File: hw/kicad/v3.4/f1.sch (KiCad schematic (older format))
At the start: 15 parts

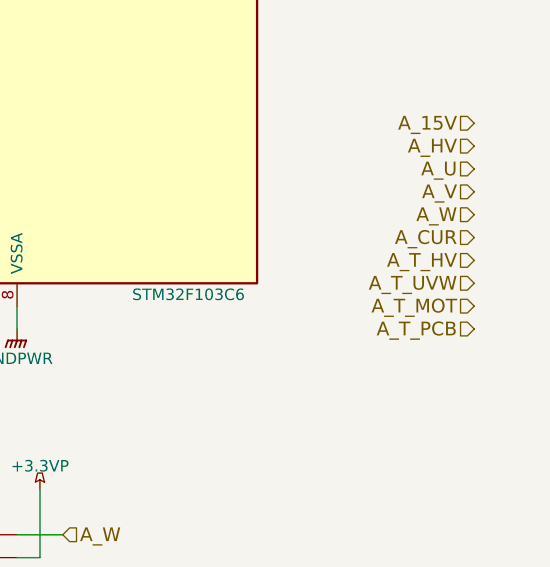
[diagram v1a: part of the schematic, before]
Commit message: +iram256
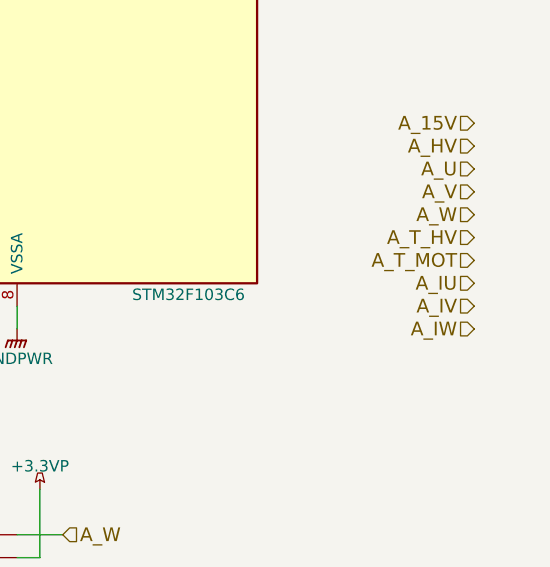
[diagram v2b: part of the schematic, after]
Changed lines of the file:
@@
 $Descr A4 11693 8268
 encoding utf-8
-Sheet 3 14
+Sheet 3 15
 Title ""
 Date ""
@@
 Text HLabel 8000 4900 0    60   Input ~ 0
 A_W
+Text HLabel 8000 5200 0    60   Input ~ 0
+A_IU
 Text HLabel 8000 5000 0    60   Input ~ 0
-A_CUR
+A_T_HV
 Text HLabel 8000 5100 0    60   Input ~ 0
-A_T_HV
-Text HLabel 8000 5200 0    60   Input ~ 0
-A_T_UVW
-Text HLabel 8000 5300 0    60   Input ~ 0
 A_T_MOT
-Text HLabel 8000 5400 0    60   Input ~ 0
-A_T_PCB
 Text HLabel 7400 3400 2    60   Input ~ 0
 HV_EN
@@
 	0    1    1    0
 $EndComp
+Text HLabel 8000 5300 0    60   Input ~ 0
+A_IV
+Text HLabel 8000 5400 0    60   Input ~ 0
+A_IW
 $EndSCHEMATC

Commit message: hw v3.4
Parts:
- added U?: USBLC6-4SC6, symbol USBLC6-4SC6
- R?: value 1k -> 10k
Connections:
- net +3.3VP: now also U?.5 (VBUS)
- net A_IU: now also U?.1 (I/O1)
- net A_IV: now also U?.3 (I/O2)
- net A_IW: now also U?.6 (I/O4)
- net A_T_MOT: now also U?.4 (I/O3)
- net GNDPWR: now also U?.2 (GND)
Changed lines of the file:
@@
 EESchema Schematic File Version 2
 LIBS:conn
+LIBS:power
 LIBS:stmbl_3.4-cache
 EELAYER 25 0
@@
 	1    0    0    -1
 $EndComp
-Wire Wire Line
-	5400 1700 5400 1900
-Wire Wire Line
-	5500 1700 5500 1900
-Wire Wire Line
-	5700 1700 5700 1900
-Wire Wire Line
-	6000 1700 6000 1900
-Wire Wire Line
-	5150 1400 6000 1400
-Connection ~ 5700 1400
-Connection ~ 5500 1400
 $Comp
 L GNDPWR #PWR?
@@
 	1    0    0    -1
 $EndComp
-Wire Wire Line
-	5150 1500 5150 1400
-Connection ~ 5400 1400
 $Comp
 L +3.3VP #PWR?
@@
 	1    0    0    -1
 $EndComp
-Wire Wire Line
-	6200 1700 6200 1800
-Wire Wire Line
-	6200 1800 6000 1800
-Connection ~ 6000 1800
 $Comp
 L C C?
@@
 	0    1    1    0
 $EndComp
-Wire Wire Line
-	3400 2800 3500 2800
-Wire Wire Line
-	3400 2500 3500 2500
-Wire Wire Line
-	3800 2500 4100 2500
-Wire Wire Line
-	3800 2800 4100 2800
-Wire Wire Line
-	4100 2800 4100 2700
-Wire Wire Line
-	4100 2700 4200 2700
-Connection ~ 3900 2800
-Wire Wire Line
-	4200 2600 4100 2600
-Wire Wire Line
-	4100 2600 4100 2500
-Connection ~ 3900 2500
 $Comp
 L C C?
@@
 	1    0    0    -1
 $EndComp
-Wire Wire Line
-	3500 2900 4200 2900
-Wire Wire Line
-	3500 2900 3500 3050
 $Comp
 L GNDPWR #PWR?
@@
 	1    0    0    -1
 $EndComp
-Wire Wire Line
-	3500 3450 3500 3350
 $Comp
 L +3.3VP #PWR?
@@
 	-1   0    0    1
 $EndComp
-Wire Wire Line
-	3800 3000 3800 2900
-Connection ~ 3800 2900
 $Comp
 L C C?
@@
 	0    1    1    0
 $EndComp
-Wire Wire Line
-	4000 2200 4200 2200
 $Comp
 L GNDPWR #PWR?
@@
 	0    1    1    0
 $EndComp
-Wire Wire Line
-	3500 2200 3700 2200
 Text HLabel 4000 4800 0    60   Input ~ 0
 CH1N
@@
 	0    1    1    0
 $EndComp
-Wire Wire Line
-	7800 1200 7800 3500
-Wire Wire Line
-	7800 1200 4100 1200
-Wire Wire Line
-	4100 1200 4100 2200
-Connection ~ 4100 2200
-Wire Wire Line
-	7200 3100 7400 3100
-Wire Wire Line
-	7200 3200 7400 3200
-Wire Wire Line
-	7200 3300 7400 3300
-Wire Wire Line
-	4000 4800 4200 4800
-Wire Wire Line
-	4000 4900 4200 4900
-Wire Wire Line
-	4000 5000 4200 5000
-Wire Wire Line
-	4000 4100 4200 4100
-Wire Wire Line
-	4000 4200 4200 4200
-Wire Wire Line
-	6000 5400 6000 5300
-Wire Wire Line
-	5700 5400 5700 5300
-Wire Wire Line
-	5500 5400 5500 5300
-Wire Wire Line
-	5400 5400 5400 5300
 Text HLabel 8000 4500 0    60   Input ~ 0
 A_15V
@@
 Text HLabel 4000 4700 0    60   Input ~ 0
 BKIN
-Wire Wire Line
-	4000 4700 4200 4700
-Wire Wire Line
-	7400 3400 7200 3400
-Wire Wire Line
-	7700 3700 7900 3700
-Wire Wire Line
-	7900 3800 7400 3800
-Wire Wire Line
-	7400 3800 7400 3700
-Wire Wire Line
-	7400 3700 7200 3700
-Wire Wire Line
-	7900 3600 7200 3600
-Wire Wire Line
-	7800 3500 7900 3500
-Wire Wire Line
-	7200 3500 7400 3500
 $Comp
 L USBLC6-4SC6 U?
@@
 Text HLabel 6200 6500 2    60   Input ~ 0
 A_HV
-Wire Wire Line
-	3700 6300 3900 6300
-Wire Wire Line
-	3700 6500 3900 6500
-Wire Wire Line
-	6000 6300 6200 6300
-Wire Wire Line
-	6000 6500 6200 6500
 $Comp
 L GNDPWR #PWR?
@@
 	1    0    0    -1
 $EndComp
-Wire Wire Line
-	6000 6400 6100 6400
-Wire Wire Line
-	6100 6400 6100 6100
-Wire Wire Line
-	3800 6700 3800 6400
-Wire Wire Line
-	3800 6400 3900 6400
 $Comp
 L C C?
@@
 	1    0    0    -1
 $EndComp
-Wire Wire Line
-	3100 6250 3100 6100
-Wire Wire Line
-	3100 6700 3100 6550
 $Comp
 L R R?
@@
 P 2900 2650
 F 0 "R?" V 2980 2650 50  0000 C CNN
-F 1 "1k" V 2900 2650 50  0000 C CNN
+F 1 "10k" V 2900 2650 50  0000 C CNN
 F 2 "" V 2830 2650 30  0000 C CNN
 F 3 "" H 2900 2650 30  0000 C CNN
@@
 	1    0    0    -1
 $EndComp
-Wire Wire Line
-	4200 2400 2900 2400
-Wire Wire Line
-	2900 2300 2900 2500
-Connection ~ 2900 2400
 $Comp
 L GNDPWR #PWR?
@@
 	1    0    0    -1
 $EndComp
-Wire Wire Line
-	2900 2800 2900 2900
 $Comp
 L +3.3VP #PWR?
@@
 	1    0    0    -1
 $EndComp
-Wire Wire Line
-	2900 2100 2900 2000
 $Comp
 L Jumper_NO_Small JP?
@@
 Text HLabel 8000 5400 0    60   Input ~ 0
 A_IW
+$Comp
+L USBLC6-4SC6 U?
+U 1 1 56820F0C
+P 4950 7200
+F 0 "U?" H 4251 7548 50  0000 C CNN
+F 1 "USBLC6-4SC6" H 4950 7450 50  0000 C CNN
+F 2 "" H 4950 7200 60  0000 C CNN
+F 3 "" H 4950 7200 60  0000 C CNN
+F 4 "TRANSIENT VOLTAGE SUPPRESSOR" H 4950 6950 50  0000 C CNN "Description"
+	1    4950 7200
+	1    0    0    -1
+$EndComp
+$Comp
+L GNDPWR #PWR?
+U 1 1 56821409
+P 3800 7400
+F 0 "#PWR?" H 3800 7200 50  0001 C CNN
+F 1 "GNDPWR" H 3800 7270 50  0000 C CNN
+F 2 "" H 3800 7350 60  0000 C CNN
+F 3 "" H 3800 7350 60  0000 C CNN
+	1    3800 7400
+	1    0    0    -1
+$EndComp
+$Comp
+L +3.3VP #PWR?
+U 1 1 56821444
+P 6100 7000
+F 0 "#PWR?" H 6250 6950 50  0001 C CNN
+F 1 "+3.3VP" H 6100 7100 50  0000 C CNN
+F 2 "" H 6100 7000 60  0000 C CNN
+F 3 "" H 6100 7000 60  0000 C CNN
+	1    6100 7000
+	1    0    0    -1
+$EndComp
+Text HLabel 3700 7100 0    60   Input ~ 0
+A_IU
+Text HLabel 3700 7300 0    60   Input ~ 0
+A_IV
+Text HLabel 6200 7100 2    60   Input ~ 0
+A_IW
+Text HLabel 6200 7300 2    60   Input ~ 0
+A_T_MOT
+Wire Wire Line
+	6000 7300 6200 7300
+Wire Wire Line
+	3700 7300 3900 7300
+Wire Wire Line
+	3700 7100 3900 7100
+Wire Wire Line
+	6000 7100 6200 7100
+Wire Wire Line
+	3800 7200 3800 7400
+Wire Wire Line
+	3900 7200 3800 7200
+Wire Wire Line
+	6100 7200 6100 7000
+Wire Wire Line
+	6000 7200 6100 7200
+Wire Wire Line
+	2900 2100 2900 2000
+Wire Wire Line
+	2900 2800 2900 2900
+Connection ~ 2900 2400
+Wire Wire Line
+	2900 2300 2900 2500
+Wire Wire Line
+	4200 2400 2900 2400
+Wire Wire Line
+	3100 6700 3100 6550
+Wire Wire Line
+	3100 6250 3100 6100
+Wire Wire Line
+	3800 6400 3900 6400
+Wire Wire Line
+	3800 6700 3800 6400
+Wire Wire Line
+	6100 6400 6100 6100
+Wire Wire Line
+	6000 6400 6100 6400
+Wire Wire Line
+	6000 6500 6200 6500
+Wire Wire Line
+	6000 6300 6200 6300
+Wire Wire Line
+	3700 6500 3900 6500
+Wire Wire Line
+	3700 6300 3900 6300
+Wire Wire Line
+	7200 3500 7400 3500
+Wire Wire Line
+	7800 3500 7900 3500
+Wire Wire Line
+	7900 3600 7200 3600
+Wire Wire Line
+	7400 3700 7200 3700
+Wire Wire Line
+	7400 3800 7400 3700
+Wire Wire Line
+	7900 3800 7400 3800
+Wire Wire Line
+	7700 3700 7900 3700
+Wire Wire Line
+	7400 3400 7200 3400
+Wire Wire Line
+	4000 4700 4200 4700
+Wire Wire Line
+	5400 5400 5400 5300
+Wire Wire Line
+	5500 5400 5500 5300
+Wire Wire Line
+	5700 5400 5700 5300
+Wire Wire Line
+	6000 5400 6000 5300
+Wire Wire Line
+	4000 4200 4200 4200
+Wire Wire Line
+	4000 4100 4200 4100
+Wire Wire Line
+	4000 5000 4200 5000
+Wire Wire Line
+	4000 4900 4200 4900
+Wire Wire Line
+	4000 4800 4200 4800
+Wire Wire Line
+	7200 3300 7400 3300
+Wire Wire Line
+	7200 3200 7400 3200
+Wire Wire Line
+	7200 3100 7400 3100
+Connection ~ 4100 2200
+Wire Wire Line
+	4100 1200 4100 2200
+Wire Wire Line
+	7800 1200 4100 1200
+Wire Wire Line
+	7800 1200 7800 3500
+Wire Wire Line
+	3500 2200 3700 2200
+Wire Wire Line
+	4000 2200 4200 2200
+Connection ~ 3800 2900
+Wire Wire Line
+	3800 3000 3800 2900
+Wire Wire Line
+	3500 3450 3500 3350
+Wire Wire Line
+	3500 2900 3500 3050
+Wire Wire Line
+	3500 2900 4200 2900
+Connection ~ 3900 2500
+Wire Wire Line
+	4100 2600 4100 2500
+Wire Wire Line
+	4200 2600 4100 2600
+Connection ~ 3900 2800
+Wire Wire Line
+	4100 2700 4200 2700
+Wire Wire Line
+	4100 2800 4100 2700
+Wire Wire Line
+	3800 2800 4100 2800
+Wire Wire Line
+	3800 2500 4100 2500
+Wire Wire Line
+	3400 2500 3500 2500
+Wire Wire Line
+	3400 2800 3500 2800
+Connection ~ 6000 1800
+Wire Wire Line
+	6200 1800 6000 1800
+Wire Wire Line
+	6200 1700 6200 1800
+Connection ~ 5400 1400
+Wire Wire Line
+	5150 1500 5150 1400
+Connection ~ 5500 1400
+Connection ~ 5700 1400
+Wire Wire Line
+	5150 1400 6000 1400
+Wire Wire Line
+	6000 1700 6000 1900
+Wire Wire Line
+	5700 1700 5700 1900
+Wire Wire Line
+	5500 1700 5500 1900
+Wire Wire Line
+	5400 1700 5400 1900
 $EndSCHEMATC

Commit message: hw v3.4 +testpoints
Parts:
- added C?: 1n, symbol C
- added R?: 1k, symbol R
- added R?: 10k, symbol R
- added T?: testpoint, symbol testpoint
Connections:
- net A_15V: now also C?.1, R?.1, R?.2, T?.1
- net GNDPWR: now also C?.2, R?.2
- new net +15V: R?.1
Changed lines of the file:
@@
 EESchema Schematic File Version 2
-LIBS:conn
 LIBS:power
 LIBS:stmbl_3.4-cache
@@
 	0    1    1    0
 $EndComp
-Text HLabel 8000 4500 0    60   Input ~ 0
-A_15V
 Text HLabel 8000 4600 0    60   Input ~ 0
 A_HV
@@
 	3800 2800 4100 2800
 Wire Wire Line
-	3800 2500 4100 2500
+	4100 2500 3800 2500
 Wire Wire Line
 	3400 2500 3500 2500
@@
 Wire Wire Line
 	5400 1700 5400 1900
+$Comp
+L R R?
+U 1 1 5682634B
+P 9300 4950
+F 0 "R?" V 9380 4950 50  0000 C CNN
+F 1 "1k" V 9300 4950 50  0000 C CNN
+F 2 "" V 9230 4950 30  0000 C CNN
+F 3 "" H 9300 4950 30  0000 C CNN
+	1    9300 4950
+	1    0    0    -1
+$EndComp
+$Comp
+L GNDPWR #PWR?
+U 1 1 568263AB
+P 9300 5300
+F 0 "#PWR?" H 9300 5100 50  0001 C CNN
+F 1 "GNDPWR" H 9300 5170 50  0000 C CNN
+F 2 "" H 9300 5250 60  0000 C CNN
+F 3 "" H 9300 5250 60  0000 C CNN
+	1    9300 5300
+	1    0    0    -1
+$EndComp
+$Comp
+L R R?
+U 1 1 568264D7
+P 9300 4450
+F 0 "R?" V 9380 4450 50  0000 C CNN
+F 1 "10k" V 9300 4450 50  0000 C CNN
+F 2 "" V 9230 4450 30  0000 C CNN
+F 3 "" H 9300 4450 30  0000 C CNN
+	1    9300 4450
+	1    0    0    -1
+$EndComp
+$Comp
+L +15V #PWR?
+U 1 1 56826605
+P 9300 4200
+F 0 "#PWR?" H 9300 4050 50  0001 C CNN
+F 1 "+15V" H 9300 4340 50  0000 C CNN
+F 2 "" H 9300 4200 50  0000 C CNN
+F 3 "" H 9300 4200 50  0000 C CNN
+	1    9300 4200
+	1    0    0    -1
+$EndComp
+Wire Wire Line
+	9300 4200 9300 4300
+Wire Wire Line
+	9300 4600 9300 4800
+Wire Wire Line
+	9300 5100 9300 5300
+Text HLabel 9200 4700 0    60   Input ~ 0
+A_15V
+Wire Wire Line
+	9200 4700 9600 4700
+Connection ~ 9300 4700
+$Comp
+L C C?
+U 1 1 568272A5
+P 9500 4950
+F 0 "C?" H 9525 5050 50  0000 L CNN
+F 1 "1n" H 9525 4850 50  0000 L CNN
+F 2 "" H 9538 4800 30  0000 C CNN
+F 3 "" H 9500 4950 60  0000 C CNN
+	1    9500 4950
+	1    0    0    -1
+$EndComp
+Wire Wire Line
+	9500 4700 9500 4800
+Wire Wire Line
+	9500 5100 9500 5200
+Wire Wire Line
+	9500 5200 9300 5200
+Connection ~ 9300 5200
+$Comp
+L testpoint T?
+U 1 1 56827AA7
+P 9800 4700
+F 0 "T?" H 9800 4800 60  0000 C CNN
+F 1 "testpoint" H 9800 4600 60  0000 C CNN
+F 2 "" H 9800 4700 60  0000 C CNN
+F 3 "" H 9800 4700 60  0000 C CNN
+	1    9800 4700
+	1    0    0    -1
+$EndComp
+Connection ~ 9500 4700
 $EndSCHEMATC

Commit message: v3.4
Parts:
- removed U?: STM32F103C6, LQFP48, symbol STM32F103C6
- added R?: 1k, symbol R
- added U?: STM32F303CBTx, LQFP48, symbol STM32F303CBTx
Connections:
- net +3.3VP: now also C?.2, C?.2, C?.2, U?.1 (VBAT), U?.24 (VDD), U?.36 (VDD), U?.48 (VDD), U?.9 (VDDA)
- net BKIN: now also U?.25 (PB12/ADC4_IN3/COMP3_INM/I2C2_SMBA/I2S2_WS/OPAMP4_VOUT/SPI2_NSS/TIM1_BKIN/TSC_G6_IO2/USART3_CK)
- net CH1: now also U?.29 (COMP3_OUT/I2C2_SMBA/I2S2_MCK/RCC_MCO/TIM1_CH1/TIM4_ETR/USART1_CK/PA8)
- net CH1N: now also U?.26 (PB13/ADC3_IN5/COMP5_INP/I2S2_CK/OPAMP3_VINP/OPAMP3_VINP_SEC/OPAMP4_VINP/OPAMP4_VINP_SEC/SPI2_SCK/TIM1_CH1N/TSC_G6_IO3/USART3_CTS)
- net CH2: now also U?.30 (COMP5_OUT/DAC_EXTI9/I2C2_SCL/I2S3_MCK/TIM15_BKIN/TIM1_CH2/TIM2_CH3/TSC_G4_IO1/USART1_TX/PA9)
- net CH2N: now also U?.27 (PB14/ADC4_IN4/COMP3_INP/I2S2_ext_SD/OPAMP2_VINP/OPAMP2_VINP_SEC/SPI2_MISO/TIM15_CH1/TIM1_CH2N/TSC_G6_IO4/USART3_DE/USART3_RTS)
- net CH3: now also U?.31 (COMP6_OUT/I2C2_SDA/TIM17_BKIN/TIM1_CH3/TIM2_CH4/TIM8_BKIN/TSC_G4_IO2/USART1_RX/PA10)
- net CH3N: now also U?.28 (PB15/ADC1_EXTI15/ADC2_EXTI15/ADC4_IN5/COMP6_INM/I2S2_SD/RTC_REFIN/SPI2_MOSI/TIM15_CH1N/TIM15_CH2/TIM1_CH3N)
- net GNDPWR: now also U?.23 (VSS), U?.35 (VSS), U?.47 (VSS), U?.8 (VSSA)
- net HV_EN: now also R?.1
- net HV_FLT: now also U?.33 (CAN_TX/COMP2_OUT/TIM16_CH1/TIM1_CH2N/TIM1_ETR/TIM4_CH2/USART1_DE/USART1_RTS/USB_DP/PA12)
- net HV_RX: now also U?.43 (PB7/I2C1_SDA/TIM17_CH1N/TIM3_CH4/TIM4_CH2/TIM8_BKIN/TSC_G5_IO4/USART1_RX)
- net HV_TX: now also U?.42 (PB6/I2C1_SCL/TIM16_CH1N/TIM4_CH1/TIM8_BKIN2/TIM8_CH1/TIM8_ETR/TSC_G5_IO3/USART1_TX)
- net at P?.3 (P3): now also U?.34 (IR_OUT/SYS_JTMS-SWDIO/TIM16_CH1N/TIM4_CH3/TSC_G4_IO3/USART3_CTS/PA13)
- net at P?.1 (P1): now also U?.37 (I2C1_SDA/SYS_JTCK-SWCLK/TIM1_BKIN/TIM8_CH2/TSC_G4_IO4/USART2_TX/PA14)
- net at JP?.2, R?.1: now also U?.44 (BOOT0)
- net at C?.1, Y?.1: now also U?.5 (PF0/I2C2_SDA/RCC_OSC_IN/TIM1_CH3N)
- net at C?.1, Y?.2: now also U?.6 (PF1/I2C2_SCL/RCC_OSC_OUT)
- net at C?.1: now also U?.7 (NRST); no longer P?.4 (P4)
- new net: R?.2, U?.32 (ADC1_EXTI11/ADC2_EXTI11/CAN_RX/COMP1_OUT/TIM1_BKIN2/TIM1_CH1N/TIM1_CH4/TIM4_CH1/USART1_CTS/USB_DM/PA11)
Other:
- moved on the sheet: C?, JP?, P?, R?, T?, U?, Y?
